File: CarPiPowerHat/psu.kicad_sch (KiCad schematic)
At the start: 43 parts, among them IC1 AP2331TDSA-7, J10 Conn_01x02_Male, J5 USB_A, Q1 DMMT5401, Q2 DMG2305UX, Q3 DMP3013SFV-7, U1 AP64501SP-13

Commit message: updated layout
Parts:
- D3: footprint Diode_SMD:D_SMB -> Diode_SMD:D_SMA_Handsoldering
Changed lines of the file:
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@@
-(kicad_sch (version 20210126) (generator eeschema)
+(kicad_sch (version 20210406) (generator eeschema)
   (paper "A4")
   (junction (at 39.37 156.21) (diameter 1.016) (color 0 0 0 0))
@@
       (effects (font (size 1.27 1.27)) (justify right))
     )
-    (property "Footprint" "Diode_SMD:D_SMB" (id 2) (at 55.245 45.72 0)
-      (effects (font (size 1.27 1.27)) hide)
-    )
+    (property "Footprint" "Diode_SMD:D_SMA_Handsoldering" (id 2) (at 55.245 45.72 0)
+      (effects (font (size 1.27 1.27)) hide)
+    )

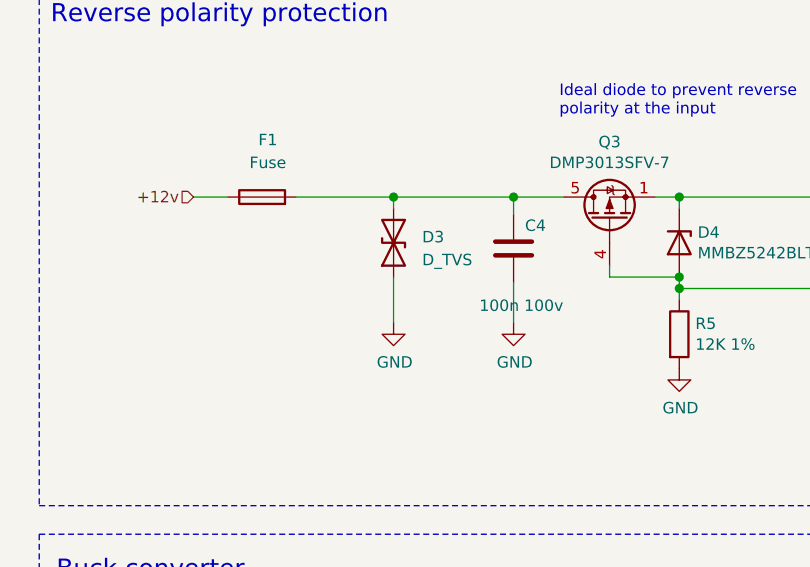
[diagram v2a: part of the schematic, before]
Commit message: Removed TVS diodes for now, fixed DRC issues
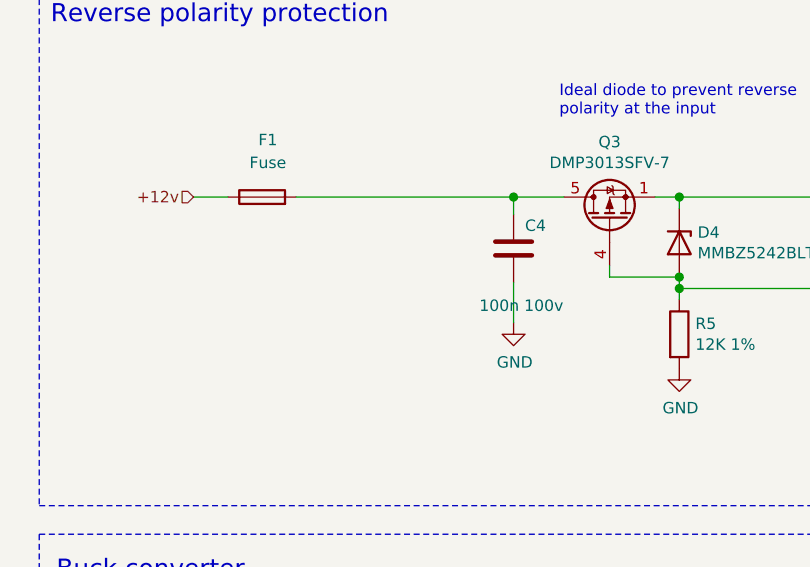
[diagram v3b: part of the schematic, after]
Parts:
- removed D3: D_TVS, Diode_SMD:D_SMA_Handsoldering, symbol Device:D_TVS
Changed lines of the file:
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@@
   (junction (at 52.07 112.395) (diameter 1.016) (color 0 0 0 0))
   (junction (at 52.07 120.015) (diameter 1.016) (color 0 0 0 0))
-  (junction (at 55.245 40.64) (diameter 1.016) (color 0 0 0 0))
   (junction (at 61.595 170.18) (diameter 1.016) (color 0 0 0 0))
   (junction (at 62.865 112.395) (diameter 1.016) (color 0 0 0 0))
@@
     (stroke (width 0) (type solid) (color 0 0 0 0))
   )
-  (wire (pts (xy 44.45 40.64) (xy 55.245 40.64))
+  (wire (pts (xy 44.45 40.64) (xy 68.58 40.64))
     (stroke (width 0) (type solid) (color 0 0 0 0))
   )
@@
   )
   (wire (pts (xy 52.07 120.015) (xy 62.865 120.015))
-    (stroke (width 0) (type solid) (color 0 0 0 0))
-  )
-  (wire (pts (xy 55.245 40.64) (xy 55.245 41.91))
-    (stroke (width 0) (type solid) (color 0 0 0 0))
-  )
-  (wire (pts (xy 55.245 40.64) (xy 68.58 40.64))
-    (stroke (width 0) (type solid) (color 0 0 0 0))
-  )
-  (wire (pts (xy 55.245 49.53) (xy 55.245 54.61))
     (stroke (width 0) (type solid) (color 0 0 0 0))
   )
@@
     (pin "1")
   )
-  (symbol (lib_id "power:GND") (at 55.245 54.61 0) (unit 1)
-    (in_bom yes) (on_board yes)
-    (property "Reference" "#PWR02" (id 0) (at 55.245 60.96 0)
-      (effects (font (size 1.27 1.27)) hide)
-    )
-    (property "Value" "GND" (id 1) (at 55.372 59.0042 0))
-    (property "Footprint" "" (id 2) (at 55.245 54.61 0)
-      (effects (font (size 1.27 1.27)) hide)
-    )
-    (property "Datasheet" "" (id 3) (at 55.245 54.61 0)
-      (effects (font (size 1.27 1.27)) hide)
-    )
-    (pin "1")
-  )
   (symbol (lib_id "power:GND") (at 61.595 177.8 0) (unit 1)
     (in_bom yes) (on_board yes)
@@
       (effects (font (size 1.27 1.27)) hide)
     )
-    (pin "1")
-    (pin "2")
-  )
-  (symbol (lib_id "Device:D_TVS") (at 55.245 45.72 90) (unit 1)
-    (in_bom yes) (on_board yes)
-    (property "Reference" "D3" (id 0) (at 58.42 45.085 90)
-      (effects (font (size 1.27 1.27)) (justify right))
-    )
-    (property "Value" "D_TVS" (id 1) (at 58.42 47.625 90)
-      (effects (font (size 1.27 1.27)) (justify right))
-    )
-    (property "Footprint" "Diode_SMD:D_SMA_Handsoldering" (id 2) (at 55.245 45.72 0)
-      (effects (font (size 1.27 1.27)) hide)
-    )
-    (property "Datasheet" "~" (id 3) (at 55.245 45.72 0)
-      (effects (font (size 1.27 1.27)) hide)
-    )

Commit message: Finished Layout
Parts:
- added D3: SMBJ33A, Diode_SMD:D_SMB, symbol Diode:SM6T6V8A
- C1, C11, C2, C3, C5, C6, C7: value 10u 35v -> 10uF 35v
- C12: Field4 (none) -> Do not populate
- C15, C16, C17, C18: value 10u -> 10uF
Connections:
- net GND: now also D3.2 (A2)
- net at C4.1, F1.2, Q3.5 (D): now also D3.1 (A1)
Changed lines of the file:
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@@
   (junction (at 41.275 112.395) (diameter 1.016) (color 0 0 0 0))
   (junction (at 41.275 120.015) (diameter 1.016) (color 0 0 0 0))
+  (junction (at 49.53 40.64) (diameter 1.016) (color 0 0 0 0))
   (junction (at 52.07 112.395) (diameter 1.016) (color 0 0 0 0))
   (junction (at 52.07 120.015) (diameter 1.016) (color 0 0 0 0))
@@
   (junction (at 83.82 120.015) (diameter 1.016) (color 0 0 0 0))
   (junction (at 86.995 40.64) (diameter 1.016) (color 0 0 0 0))
-  (junction (at 86.995 49.53) (diameter 1.016) (color 0 0 0 0))
-  (junction (at 86.995 50.8) (diameter 1.016) (color 0 0 0 0))
+  (junction (at 86.995 51.435) (diameter 1.016) (color 0 0 0 0))
   (junction (at 95.25 112.395) (diameter 1.016) (color 0 0 0 0))
   (junction (at 95.25 120.015) (diameter 1.016) (color 0 0 0 0))
@@
     (stroke (width 0) (type solid) (color 0 0 0 0))
   )
-  (wire (pts (xy 44.45 40.64) (xy 68.58 40.64))
+  (wire (pts (xy 44.45 40.64) (xy 49.53 40.64))
+    (stroke (width 0) (type solid) (color 0 0 0 0))
+  )
+  (wire (pts (xy 49.53 40.64) (xy 49.53 42.545))
+    (stroke (width 0) (type solid) (color 0 0 0 0))
+  )
+  (wire (pts (xy 49.53 40.64) (xy 68.58 40.64))
+    (stroke (width 0) (type solid) (color 0 0 0 0))
+  )
+  (wire (pts (xy 49.53 50.165) (xy 49.53 54.61))
     (stroke (width 0) (type solid) (color 0 0 0 0))
   )
@@
     (stroke (width 0) (type solid) (color 0 0 0 0))
   )
-  (wire (pts (xy 79.248 48.26) (xy 79.248 49.53))
-    (stroke (width 0) (type solid) (color 0 0 0 0))
-  )
-  (wire (pts (xy 79.248 49.53) (xy 86.995 49.53))
+  (wire (pts (xy 79.248 48.26) (xy 79.248 51.435))
+    (stroke (width 0) (type solid) (color 0 0 0 0))
+  )
+  (wire (pts (xy 79.248 51.435) (xy 86.995 51.435))
     (stroke (width 0) (type solid) (color 0 0 0 0))
   )
@@
     (stroke (width 0) (type solid) (color 0 0 0 0))
   )
-  (wire (pts (xy 86.995 49.53) (xy 86.995 50.8))
-    (stroke (width 0) (type solid) (color 0 0 0 0))
-  )
-  (wire (pts (xy 86.995 50.8) (xy 86.995 52.07))
-    (stroke (width 0) (type solid) (color 0 0 0 0))
-  )
-  (wire (pts (xy 86.995 50.8) (xy 107.315 50.8))
+  (wire (pts (xy 86.995 49.53) (xy 86.995 51.435))
+    (stroke (width 0) (type solid) (color 0 0 0 0))
+  )
+  (wire (pts (xy 86.995 51.435) (xy 86.995 52.07))
+    (stroke (width 0) (type solid) (color 0 0 0 0))
+  )
+  (wire (pts (xy 86.995 51.435) (xy 107.315 51.435))
     (stroke (width 0) (type solid) (color 0 0 0 0))
   )
@@
     (stroke (width 0) (type solid) (color 0 0 0 0))
   )
-  (wire (pts (xy 107.315 50.8) (xy 107.315 48.895))
+  (wire (pts (xy 107.315 51.435) (xy 107.315 48.895))
     (stroke (width 0) (type solid) (color 0 0 0 0))
   )
@@
     (pin "1")
   )
+  (symbol (lib_id "power:GND") (at 49.53 54.61 0) (unit 1)
+    (in_bom yes) (on_board yes)
+    (property "Reference" "#PWR0150" (id 0) (at 49.53 60.96 0)
+      (effects (font (size 1.27 1.27)) hide)
+    )
+    (property "Value" "GND" (id 1) (at 49.657 59.0042 0))
+    (property "Footprint" "" (id 2) (at 49.53 54.61 0)
+      (effects (font (size 1.27 1.27)) hide)
+    )
+    (property "Datasheet" "" (id 3) (at 49.53 54.61 0)
+      (effects (font (size 1.27 1.27)) hide)
+    )
+    (pin "1")
+  )
   (symbol (lib_id "power:GND") (at 61.595 177.8 0) (unit 1)
     (in_bom yes) (on_board yes)
@@
     (pin "2")
   )
+  (symbol (lib_id "Diode:SM6T6V8A") (at 49.53 46.355 270) (unit 1)
+    (in_bom yes) (on_board yes) (fields_autoplaced)
+    (property "Reference" "D3" (id 0) (at 52.07 45.0849 90)
+      (effects (font (size 1.27 1.27)) (justify left))
+    )
+    (property "Value" "SMBJ33A" (id 1) (at 52.07 47.6249 90)
+      (effects (font (size 1.27 1.27)) (justify left))
+    )
+    (property "Footprint" "Diode_SMD:D_SMB" (id 2) (at 44.45 46.355 0)
+      (effects (font (size 1.27 1.27)) hide)
+    )
+    (property "Datasheet" "https://www.littelfuse.com/~/media/electronics/datasheets/tvs_diodes/littelfuse_tvs_diode_smbj_datasheet.pdf.pdf" (id 3) (at 49.53 45.085 0)
+      (effects (font (size 1.27 1.27)) hide)
+    )
+    (pin "1")
+    (pin "2")
+  )
   (symbol (lib_id "Diode:BZX84Cxx") (at 86.995 45.72 270) (unit 1)
     (in_bom yes) (on_board yes)
@@
       (effects (font (size 1.27 1.27)) (justify left))
     )
-    (property "Value" "10u 35v" (id 1) (at 37.719 121.793 0)
+    (property "Value" "10uF 35v" (id 1) (at 37.719 121.793 0)
       (effects (font (size 1.27 1.27)) (justify left))
     )
@@
       (effects (font (size 1.27 1.27)) (justify left))
     )
-    (property "Value" "10u 35v" (id 1) (at 49.022 121.793 0)
+    (property "Value" "10uF 35v" (id 1) (at 49.022 121.793 0)
       (effects (font (size 1.27 1.27)) (justify left))
     )
@@
       (effects (font (size 1.27 1.27)) (justify left))
     )
-    (property "Value" "10u 35v" (id 1) (at 59.055 121.793 0)
+    (property "Value" "10uF 35v" (id 1) (at 59.055 121.793 0)
       (effects (font (size 1.27 1.27)) (justify left))
     )
@@
       (effects (font (size 1.27 1.27)) hide)
     )
+    (property "Value" "10uF 35v" (id 11) (at 62.865 116.205 0)
+      (effects (font (size 1.27 1.27)) hide)
+    )
     (pin "1")
     (pin "2")
@@
       (effects (font (size 1.27 1.27)) (justify left))
     )
-    (property "Value" "100n 100v" (id 1) (at 64.77 52.705 0)
+    (property "Value" "100n 100v" (id 1) (at 63.5 50.165 0)
       (effects (font (size 1.27 1.27)) (justify left))
     )
@@
       (effects (font (size 1.27 1.27)) (justify left))
     )
-    (property "Value" "10u 35v" (id 1) (at 69.215 121.793 0)
+    (property "Value" "10uF 35v" (id 1) (at 69.215 121.793 0)
       (effects (font (size 1.27 1.27)) (justify left))
     )
@@
       (effects (font (size 1.27 1.27)) (justify left))
     )
-    (property "Value" "10u 35v" (id 1) (at 80.772 121.793 0)
+    (property "Value" "10uF 35v" (id 1) (at 80.772 121.793 0)
       (effects (font (size 1.27 1.27)) (justify left))
     )
@@
       (effects (font (size 1.27 1.27)) (justify left))
     )
-    (property "Value" "10u 35v" (id 1) (at 92.456 121.793 0)
+    (property "Value" "10uF 35v" (id 1) (at 92.456 121.793 0)
       (effects (font (size 1.27 1.27)) (justify left))
     )
@@
       (effects (font (size 1.27 1.27)) (justify left))
     )
-    (property "Value" "10u 35v" (id 1) (at 128.651 45.593 0)
+    (property "Value" "10uF 35v" (id 1) (at 128.651 45.593 0)
       (effects (font (size 1.27 1.27)) (justify left))
     )
@@
       (effects (font (size 1.27 1.27)) hide)
     )
-    (property "Field4" "" (id 4) (at 135.255 126.492 0)
+    (property "Field4" "Do not populate" (id 4) (at 135.255 126.492 0)
       (effects (font (size 1.27 1.27)) hide)
     )
@@
       (effects (font (size 1.27 1.27)) (justify left))
     )
-    (property "Value" "10u" (id 1) (at 187.071 103.505 0)
+    (property "Value" "10uF" (id 1) (at 187.071 103.505 0)
       (effects (font (size 1.27 1.27)) (justify left))
     )
@@
       (effects (font (size 1.27 1.27)) (justify left))
     )
-    (property "Value" "10u" (id 1) (at 197.231 103.505 0)
+    (property "Value" "10uF" (id 1) (at 197.231 103.505 0)
       (effects (font (size 1.27 1.27)) (justify left))
     )
@@
       (effects (font (size 1.27 1.27)) (justify left))
     )
-    (property "Value" "10u" (id 1) (at 207.391 103.505 0)
+    (property "Value" "10uF" (id 1) (at 207.391 103.505 0)
       (effects (font (size 1.27 1.27)) (justify left))
     )
@@
       (effects (font (size 1.27 1.27)) (justify left))
     )
-    (property "Value" "10u" (id 1) (at 216.281 103.505 0)
-      (effects (font (size 1.27 1.27)) (justify left))
-    )
+    (property "Value" "10uF" (id 1) (at 216.281 103.505 0)
+      (effects (font (size 1.27 1.27)) (justify left))
+    )

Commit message: Added part numbers
* Selected parts from lcsc
* Checked footprints
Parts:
- C10, C25, C26, C8, C9: value 100n -> 100n 16v
- C14: Field4 Farnell -> Do not populate
- C4: footprint Capacitor_SMD:C_0402_1005Metric -> Capacitor_SMD:C_0805_2012Metric; Field6 GRM155R62A104KE14D -> RM EMK105 B7104KV-F; LCSC C1525 -> C495959
- D3: LCSC (none) -> C143163
- Q1: LCSC (none) -> C154733
- Q2: value DMG2305UX -> DMG2305
- Q3: LCSC (none) -> C264098
- R1: footprint Resistor_SMD:R_0402_1005Metric_Pad0.72x0.64mm_HandSolder -> Resistor_SMD:R_0603_1608Metric; LCSC (none) -> C25804
- R4: footprint Resistor_SMD:R_0402_1005Metric_Pad0.72x0.64mm_HandSolder -> Resistor_SMD:R_0603_1608Metric; LCSC (none) -> C25819
- R5: LCSC C25879 -> C25752
- R7: LCSC (none) -> C25077
- U1: LCSC (none) -> C2071517
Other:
- title: (none) -> Power Circuit
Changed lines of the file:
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@@
 (kicad_sch (version 20210621) (generator eeschema)
   (paper "A4")
+  (title_block
+    (title "Power Circuit")
+    (date "2021-08-24")
+    (rev "2")
+  )
   (junction (at 39.37 156.21) (diameter 1.016) (color 0 0 0 0))
   (junction (at 41.275 112.395) (diameter 1.016) (color 0 0 0 0))
@@
       (effects (font (size 1.27 1.27)) hide)
     )
-    (property "LCSC" "C25879" (id 9) (at 86.995 55.88 0)
+    (property "LCSC" "C25752" (id 9) (at 86.995 55.88 0)
       (effects (font (size 1.27 1.27)) hide)
     )
@@
     )
     (property "Part Description" "Resistor 10R M1005 1% 63mW" (id 9) (at 109.855 98.552 0)
+      (effects (font (size 1.27 1.27)) hide)
+    )
+    (property "LCSC" "C25077" (id 10) (at 109.855 98.552 0)
       (effects (font (size 1.27 1.27)) hide)
     )
@@
     (property "Reference" "R1" (id 0) (at 170.942 62.23 90))
     (property "Value" "10K" (id 1) (at 168.91 62.23 90))
-    (property "Footprint" "Resistor_SMD:R_0402_1005Metric_Pad0.72x0.64mm_HandSolder" (id 2) (at 167.132 62.23 90)
+    (property "Footprint" "Resistor_SMD:R_0603_1608Metric" (id 2) (at 167.132 62.23 90)
       (effects (font (size 1.27 1.27)) hide)
     )
     (property "Datasheet" "~" (id 3) (at 168.91 62.23 0)
+      (effects (font (size 1.27 1.27)) hide)
+    )
+    (property "LCSC" "C25804" (id 4) (at 168.91 62.23 0)
       (effects (font (size 1.27 1.27)) hide)
     )
@@
     (property "Reference" "R4" (id 0) (at 191.262 62.23 90))
     (property "Value" "47K" (id 1) (at 189.23 62.23 90))
-    (property "Footprint" "Resistor_SMD:R_0402_1005Metric_Pad0.72x0.64mm_HandSolder" (id 2) (at 187.452 62.23 90)
+    (property "Footprint" "Resistor_SMD:R_0603_1608Metric" (id 2) (at 187.452 62.23 90)
       (effects (font (size 1.27 1.27)) hide)
     )
     (property "Datasheet" "~" (id 3) (at 189.23 62.23 0)
+      (effects (font (size 1.27 1.27)) hide)
+    )
+    (property "LCSC" "C25819" (id 4) (at 189.23 62.23 0)
       (effects (font (size 1.27 1.27)) hide)
     )
@@
       (effects (font (size 1.27 1.27)) hide)
     )
+    (property "LCSC" "C143163" (id 4) (at 49.53 46.355 0)
+      (effects (font (size 1.27 1.27)) hide)
+    )
     (pin "1")
     (pin "2")
@@
       (effects (font (size 1.27 1.27)) (justify left))
     )
-    (property "Value" "100n" (id 1) (at 64.516 175.133 0)
+    (property "Value" "100n 16v" (id 1) (at 64.516 175.133 0)
       (effects (font (size 1.27 1.27)) (justify left))
     )
@@
       (effects (font (size 1.27 1.27)) (justify left))
     )
-    (property "Footprint" "Capacitor_SMD:C_0402_1005Metric" (id 2) (at 69.5452 50.165 0)
+    (property "Footprint" "Capacitor_SMD:C_0805_2012Metric" (id 2) (at 69.5452 50.165 0)
       (effects (font (size 1.27 1.27)) hide)
     )
@@
       (effects (font (size 1.27 1.27)) hide)
     )
-    (property "Field6" "GRM155R62A104KE14D" (id 6) (at 68.58 46.355 0)
+    (property "Field6" "RM EMK105 B7104KV-F" (id 6) (at 68.58 46.355 0)
       (effects (font (size 1.27 1.27)) hide)
     )
@@
       (effects (font (size 1.27 1.27)) hide)
     )
-    (property "LCSC" "C1525" (id 9) (at 68.58 46.355 0)
+    (property "LCSC" "C495959" (id 9) (at 68.58 46.355 0)
       (effects (font (size 1.27 1.27)) hide)
     )
@@
       (effects (font (size 1.27 1.27)) (justify left))
     )
-    (property "Value" "100n" (id 1) (at 100.711 172.593 0)
+    (property "Value" "100n 16v" (id 1) (at 100.711 172.593 0)
       (effects (font (size 1.27 1.27)) (justify left))
     )
@@
       (effects (font (size 1.27 1.27)) (justify left))
     )
-    (property "Value" "100n" (id 1) (at 95.885 105.156 0)
+    (property "Value" "100n 16v" (id 1) (at 95.885 105.156 0)
       (effects (font (size 1.27 1.27)) (justify left))
     )
@@
       (effects (font (size 1.27 1.27)) (justify left))
     )
-    (property "Value" "100n" (id 1) (at 108.585 46.99 0)
+    (property "Value" "100n 16v" (id 1) (at 108.585 46.99 0)
       (effects (font (size 1.27 1.27)) (justify left))
     )
@@
       (effects (font (size 1.27 1.27)) (justify left))
     )
-    (property "Value" "100n" (id 1) (at 111.125 129.032 0)
+    (property "Value" "100n 16v" (id 1) (at 111.125 129.032 0)
       (effects (font (size 1.27 1.27)) (justify left))
     )
@@
       (effects (font (size 1.27 1.27)) hide)
     )
-    (property "Field4" "Farnell" (id 4) (at 165.1 109.982 0)
+    (property "Field4" "Do not populate" (id 4) (at 165.1 109.982 0)
       (effects (font (size 1.27 1.27)) hide)
     )
@@
     (property "Datasheet" "" (id 3) (at 186.69 46.99 0)
       (effects (font (size 1.27 1.27)) (justify left))
+    )
+    (property "LCSC" "C154733" (id 4) (at 186.69 46.99 0)
+      (effects (font (size 1.27 1.27)) hide)
     )
     (pin "3")
@@
       (effects (font (size 1.27 1.27)) hide)
     )
+    (property "LCSC" "C264098" (id 9) (at 79.248 43.18 0)
+      (effects (font (size 1.27 1.27)) hide)
+    )
     (pin "1")
     (pin "2")
@@
       (effects (font (size 1.27 1.27)) (justify right))
     )
-    (property "Value" "DMG2305UX" (id 1) (at 180.34 27.94 90)
+    (property "Value" "DMG2305" (id 1) (at 180.34 27.94 90)
       (effects (font (size 1.27 1.27)) (justify right))
     )
@@
       (effects (font (size 1.27 1.27)) hide)
     )
+    (property "LCSC" "C2071517" (id 9) (at 118.11 112.395 0)
+      (effects (font (size 1.27 1.27)) hide)
+    )

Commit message: Fixed some bugs, not done yet
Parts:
- added C38: 100uF, Capacitor_SMD:C_0603_1608Metric_Pad1.08x0.95mm_HandSolder, symbol Device:C
- added C39: 1uF, Capacitor_SMD:C_0603_1608Metric_Pad1.08x0.95mm_HandSolder, symbol Device:C
- added IC2: BD2226G-TR, SOT95P280X125-5N, symbol Samac_Sys:BD2226G-TR
- C10: renamed from C11; LCSC C469541 -> C162422
- C14: renamed from C1; LCSC C469541 -> C162422
- C15: renamed from C7; LCSC C469541 -> C162422
- C17: renamed from C2; LCSC C469541 -> C162422
- C18: renamed from C3; LCSC C469541 -> C162422
- C19: renamed from C5; LCSC C469541 -> C162422
- C2: renamed from C19; LCSC C16133 -> (none)
- C33: renamed from C4; LCSC C495959 -> C28233
- C8: renamed from C6; LCSC C469541 -> C162422
- D8: renamed from D3; LCSC C143163 -> C353366
- J7: renamed from J5; Mfr. No (none) -> 614004134726; Mouser No (none) -> 710-614004134726
- renumbered C12 to C11, C10 to C12, C9 to C13, C14 to C16, C25 to C26, C16 to C3, C26 to C37, C18 to C4, C15 to C5, C17 to C6, C8 to C7, C13 to C9, D4 to D2, F1 to F2, J10 to J8, Q3 to Q4, R4 to R1, R9 to R10, R7 to R11, R1 to R2, R5 to R8, R10 to R9, TP3 to TP1, TP1 to TP2, TP2 to TP3, TP5 to TP4, U1 to U3
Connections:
- net GND: now also C38.2, C39.2, IC2.2 (GND), IC2.4 (~OC)
- net P5V: now also C38.1, C39.1, IC2.1 (IN), IC2.3 (EN)
- net USB_5v: now also IC2.5 (OUT)
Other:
- note added: "BD2226G-TR C308587"
- moved on the sheet: C26, C37, IC1
